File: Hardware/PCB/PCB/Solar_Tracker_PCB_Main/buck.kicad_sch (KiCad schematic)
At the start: 13 parts, among them IC2 TPS54302DDCT

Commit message: Actualizacion PCB Principal
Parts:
- C6: value 75p -> 47p
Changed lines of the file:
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@@
 	(generator_version "9.0")
 	(paper "A4")
+	(text_box "These component values follow the typical application (Figure 8-1, page 14).\nAlternative values are listed in Table 8-2 (page 18) for 3.3 V output.\nThe typical voltage refence (Fb) is 0.596V.\n\nSpecs:\n	Use X7R ceramic capacitors\n	Use resistors with 1% maximum tolerance\n	Use ferrite-core inductors\n\n "
+		(exclude_from_sim no)
+		(at 31.75 139.7 0)
+		(size 85.09 35.56)
+		(margins 0.9525 0.9525 0.9525 0.9525)
+		(stroke
+			(width 0)
+			(type solid)
+		)
+		(fill
+			(type none)
+		)
+		(effects
+			(font
+				(size 1.27 1.27)
+			)
+			(justify left top)
+		)
+	)
 	(junction
 		(at 179.07 80.01)
@@
 		)
 		(instances
-			(project ""
+			(project "Solar_Tracker_PCB_Main"
 				(path "/99b6ddd9-7ffe-4c85-972a-e0f594a166d4/c6e05bfb-9dbb-4b23-9f99-8dd532fd7f1c"
 					(reference "IC2")
@@
 		)
 		(instances
-			(project ""
+			(project "Solar_Tracker_PCB_Main"
 				(path "/99b6ddd9-7ffe-4c85-972a-e0f594a166d4/c6e05bfb-9dbb-4b23-9f99-8dd532fd7f1c"
 					(reference "R6")
@@
 		)
 		(instances
-			(project ""
+			(project "Solar_Tracker_PCB_Main"
 				(path "/99b6ddd9-7ffe-4c85-972a-e0f594a166d4/c6e05bfb-9dbb-4b23-9f99-8dd532fd7f1c"
 					(reference "#PWR013")
@@
 		)
 		(instances
-			(project ""
+			(project "Solar_Tracker_PCB_Main"
 				(path "/99b6ddd9-7ffe-4c85-972a-e0f594a166d4/c6e05bfb-9dbb-4b23-9f99-8dd532fd7f1c"
 					(reference "L1")
@@
 			)
 		)
-		(property "Value" "75p"
+		(property "Value" "47p"
 			(at 173.736 76.962 0)
 			(effects

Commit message: Actualizacion de Footprints Resistencias y Capacitores Main PCB
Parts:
- C10, C11, C6, C7, C8, C9: footprint (none) -> Capacitor_SMD:C_0805_2012Metric_Pad1.18x1.45mm_HandSolder
- L1: footprint (none) -> Inductor_SMD:L_0805_2012Metric_Pad1.05x1.20mm_HandSolder
- R10, R6, R7, R8, R9: footprint (none) -> Resistor_SMD:R_0805_2012Metric_Pad1.20x1.40mm_HandSolder
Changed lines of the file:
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@@
 			)
 		)
-		(property "Footprint" ""
+		(property "Footprint" "Capacitor_SMD:C_0805_2012Metric_Pad1.18x1.45mm_HandSolder"
 			(at 91.1352 87.63 0)
 			(effects
@@
 			)
 		)
-		(property "Footprint" ""
+		(property "Footprint" "Capacitor_SMD:C_0805_2012Metric_Pad1.18x1.45mm_HandSolder"
 			(at 142.24 58.7248 0)
 			(effects
@@
 			)
 		)
-		(property "Footprint" ""
+		(property "Footprint" "Resistor_SMD:R_0805_2012Metric_Pad1.20x1.40mm_HandSolder"
 			(at 184.912 74.93 90)
 			(effects
@@
 			)
 		)
-		(property "Footprint" ""
+		(property "Footprint" "Resistor_SMD:R_0805_2012Metric_Pad1.20x1.40mm_HandSolder"
 			(at 184.912 63.5 90)
 			(effects
@@
 			)
 		)
-		(property "Footprint" ""
+		(property "Footprint" "Resistor_SMD:R_0805_2012Metric_Pad1.20x1.40mm_HandSolder"
 			(at 109.982 92.71 90)
 			(effects
@@
 			)
 		)
-		(property "Footprint" ""
+		(property "Footprint" "Capacitor_SMD:C_0805_2012Metric_Pad1.18x1.45mm_HandSolder"
 			(at 173.6852 67.31 0)
 			(effects
@@
 			)
 		)
-		(property "Footprint" ""
+		(property "Footprint" "Capacitor_SMD:C_0805_2012Metric_Pad1.18x1.45mm_HandSolder"
 			(at 98.7552 87.63 0)
 			(effects
@@
 			)
 		)
-		(property "Footprint" ""
+		(property "Footprint" "Capacitor_SMD:C_0805_2012Metric_Pad1.18x1.45mm_HandSolder"
 			(at 165.4048 59.69 0)
 			(effects
@@
 			)
 		)
-		(property "Footprint" ""
+		(property "Footprint" "Inductor_SMD:L_0805_2012Metric_Pad1.05x1.20mm_HandSolder"
 			(at 158.75 59.69 0)
 			(effects
@@
 			)
 		)
-		(property "Footprint" ""
+		(property "Footprint" "Resistor_SMD:R_0805_2012Metric_Pad1.20x1.40mm_HandSolder"
 			(at 109.982 83.82 90)
 			(effects
@@
 			)
 		)
-		(property "Footprint" ""
+		(property "Footprint" "Resistor_SMD:R_0805_2012Metric_Pad1.20x1.40mm_HandSolder"
 			(at 184.912 85.09 90)
 			(effects
@@
 			)
 		)
-		(property "Footprint" ""
+		(property "Footprint" "Capacitor_SMD:C_0805_2012Metric_Pad1.18x1.45mm_HandSolder"
 			(at 180.0352 77.47 0)
 			(effects

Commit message: Actualizacion Main pcb
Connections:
- net BUCK_VOUT renamed VDD
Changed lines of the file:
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@@
-		)
-	)
-	(global_label "BUCK_VOUT"
-		(shape input)
-		(at 199.39 59.69 0)
-		(fields_autoplaced yes)
-		(effects
-			(font
-				(size 1.27 1.27)
-			)
-			(justify left)
-		)
-		(property "Intersheetrefs" "${INTERSHEET_REFS}"
-			(at 213.2005 59.69 0)
-			(effects
-				(font
-					(size 1.27 1.27)
-				)
-				(justify left)
-				(hide yes)
-			)
 		)
 	)
@@
 					(unit 1)
 				)
+			)
+		)
+	)
+	(symbol
+		(lib_id "power:VDD")
+		(at 199.39 59.69 270)
+		(unit 1)
+		(exclude_from_sim no)
+		(in_bom yes)
+		(on_board yes)
+		(dnp no)
+		(fields_autoplaced yes)
+		(property "Reference" "#PWR060"
+			(at 195.58 59.69 0)
+			(effects
+				(font
+					(size 1.27 1.27)
+				)
+				(hide yes)
+			)
+		)
+		(property "Value" "VDD"
+			(at 203.2 59.6899 90)
+			(effects
+				(font
+					(size 1.27 1.27)
+				)
+				(justify left)
+			)
+		)
+		(property "Footprint" ""
+			(at 199.39 59.69 0)
+			(effects
+				(font
+					(size 1.27 1.27)
+				)
+				(hide yes)
+			)
+		)
+		(property "Datasheet" ""
+			(at 199.39 59.69 0)
+			(effects
+				(font
+					(size 1.27 1.27)
+				)
+				(hide yes)
+			)
+		)
+		(property "Description" "Power symbol creates a global label with name \"VDD\""
+			(at 199.39 59.69 0)
+			(effects
+				(font
+					(size 1.27 1.27)
+				)
+				(hide yes)
+			)
+		)
+		(pin "1"
+		)
+		(instances
+			(project "Solar_Tracker_PCB_Main"
+				(path "/99b6ddd9-7ffe-4c85-972a-e0f594a166d4/c6e05bfb-9dbb-4b23-9f99-8dd532fd7f1c"
+					(reference "#PWR060")
+					(unit 1)
+				)

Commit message: comienzo de distribucion pcb
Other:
- moved on the sheet: C10, C11, C6, C7, C8, C9, IC2, L1, R10, R6, R7, R8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

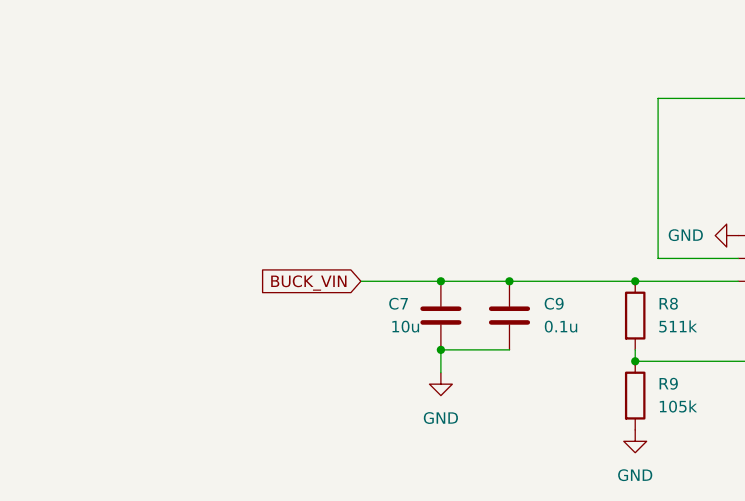
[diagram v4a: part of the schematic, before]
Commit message: Modificaciones PCB MAIN
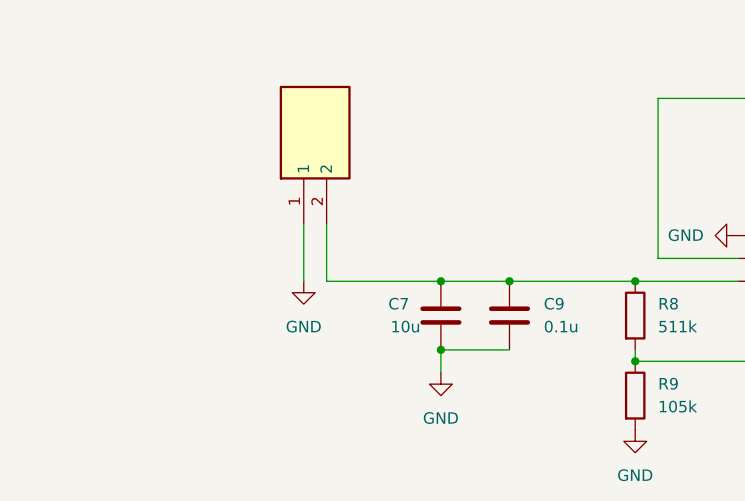
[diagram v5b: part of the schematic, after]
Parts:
- added J7: TB002-500-02BE, TB002:TB00250002BE, symbol TB002-500-02BE:TB002-500-02BE
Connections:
- net GND: now also J7.1
- net BUCK_VIN: no longer names the net of C7.1, C9.1, IC2.3 (VIN), R8.1
- net BUCK_VIN: now also J7.2
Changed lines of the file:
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@@
 	(wire
 		(pts
-			(xy 69.85 88.9) (xy 78.74 88.9)
+			(xy 66.04 88.9) (xy 66.04 82.55)
+		)
+		(stroke
+			(width 0)
+			(type default)
+		)
+	)
+	(wire
+		(pts
+			(xy 66.04 88.9) (xy 78.74 88.9)
 		)
 		(stroke
@@
 	(wire
 		(pts
+			(xy 63.5 82.55) (xy 63.5 88.9)
+		)
+		(stroke
+			(width 0)
+			(type default)
+		)
+	)
+	(wire
+		(pts
 			(xy 175.26 68.58) (xy 187.96 68.58)
 		)
@@
 			(width 0)
 			(type default)
-		)
-	)
-	(global_label "BUCK_VIN"
-		(shape input)
-		(at 69.85 88.9 180)
-		(fields_autoplaced yes)
-		(effects
-			(font
-				(size 1.27 1.27)
-			)
-			(justify right)
-		)
-		(property "Intersheetrefs" "${INTERSHEET_REFS}"
-			(at 57.7328 88.9 0)
-			(effects
-				(font
-					(size 1.27 1.27)
-				)
-				(justify right)
-				(hide yes)
-			)
 		)
 	)
@@
 	)
 	(symbol
+		(lib_id "power:GND")
+		(at 63.5 88.9 0)
+		(unit 1)
+		(exclude_from_sim no)
+		(in_bom yes)
+		(on_board yes)
+		(dnp no)
+		(fields_autoplaced yes)
+		(property "Reference" "#PWR069"
+			(at 63.5 95.25 0)
+			(effects
+				(font
+					(size 1.27 1.27)
+				)
+				(hide yes)
+			)
+		)
+		(property "Value" "GND"
+			(at 63.5 93.98 0)
+			(effects
+				(font
+					(size 1.27 1.27)
+				)
+			)
+		)
+		(property "Footprint" ""
+			(at 63.5 88.9 0)
+			(effects
+				(font
+					(size 1.27 1.27)
+				)
+				(hide yes)
+			)
+		)
+		(property "Datasheet" ""
+			(at 63.5 88.9 0)
+			(effects
+				(font
+					(size 1.27 1.27)
+				)
+				(hide yes)
+			)
+		)
+		(property "Description" "Power symbol creates a global label with name \"GND\" , ground"
+			(at 63.5 88.9 0)
+			(effects
+				(font
+					(size 1.27 1.27)
+				)
+				(hide yes)
+			)
+		)
+		(pin "1"
+		)
+		(instances
+			(project "Solar_Tracker_PCB_Main"
+				(path "/99b6ddd9-7ffe-4c85-972a-e0f594a166d4/c6e05bfb-9dbb-4b23-9f99-8dd532fd7f1c"
+					(reference "#PWR069")
+					(unit 1)
+				)
+			)
+		)
+	)
+	(symbol
 		(lib_id "Device:C")
 		(at 78.74 92.71 0)
@@
 					(unit 1)
 				)
+			)
+		)
+	)
+	(symbol
+		(lib_id "TB002-500-02BE:TB002-500-02BE")
+		(at 63.5 82.55 90)
+		(unit 1)
+		(exclude_from_sim no)
+		(in_bom yes)
+		(on_board yes)
+		(dnp no)
+		(fields_autoplaced yes)
+		(property "Reference" "J7"
+			(at 63.4999 66.04 0)
+			(effects
+				(font
+					(size 1.27 1.27)
+				)
+				(justify left)
+				(hide yes)
+			)
+		)
+		(property "Value" "TB002-500-02BE"
+			(at 66.0399 66.04 0)
+			(effects
+				(font
+					(size 1.27 1.27)
+				)
+				(justify left)
+				(hide yes)
+			)
+		)
+		(property "Footprint" "TB002:TB00250002BE"
+			(at 158.42 66.04 0)
+			(effects
+				(font
+					(size 1.27 1.27)
+				)
+				(justify left top)
+				(hide yes)
+			)
+		)
+		(property "Datasheet" "https://www.sameskydevices.com/product/resource/tb002-500.pdf"
+			(at 258.42 66.04 0)
+			(effects
+				(font
+					(size 1.27 1.27)
+				)
+				(justify left top)
+				(hide yes)
+			)
+		)
+		(property "Description" "TB002-500 Series - 2~24 Poles, Screw Type, Horizontal, 5.0 Pitch, 22~12 (AWG), Terminal Block Connector"
+			(at 63.5 82.55 0)
+			(effects
+				(font
+					(size 1.27 1.27)
+				)
+				(hide yes)
+			)
+		)
+		(property "Height" "10.4"
+			(at 458.42 66.04 0)
+			(effects
+				(font
+					(size 1.27 1.27)
+				)
+				(justify left top)
+				(hide yes)
+			)
+		)
+		(property "Mouser Part Number" "490-TB002-500-02BE"
+			(at 558.42 66.04 0)
+			(effects
+				(font
+					(size 1.27 1.27)
+				)
+				(justify left top)
+				(hide yes)
+			)
+		)
+		(property "Mouser Price/Stock" "https://www.mouser.co.uk/ProductDetail/Same-Sky/TB002-500-02BE?qs=vLWxofP3U2x9716kcgva%2Fw%3D%3D"
+			(at 658.42 66.04 0)
+			(effects
+				(font
+					(size 1.27 1.27)
+				)
+				(justify left top)
+				(hide yes)
+			)
+		)
+		(property "Manufacturer_Name" "Same Sky"
+			(at 758.42 66.04 0)
+			(effects
+				(font
+					(size 1.27 1.27)
+				)
+				(justify left top)
+				(hide yes)
+			)
+		)
+		(property "Manufacturer_Part_Number" "TB002-500-02BE"
+			(at 858.42 66.04 0)
+			(effects
+				(font
+					(size 1.27 1.27)
+				)
+				(justify left top)
+				(hide yes)
+			)
+		)
+		(pin "2"
+		)
+		(pin "1"
+		)
+		(instances
+			(project ""
+				(path "/99b6ddd9-7ffe-4c85-972a-e0f594a166d4/c6e05bfb-9dbb-4b23-9f99-8dd532fd7f1c"
+					(reference "J7")
+					(unit 1)
+				)

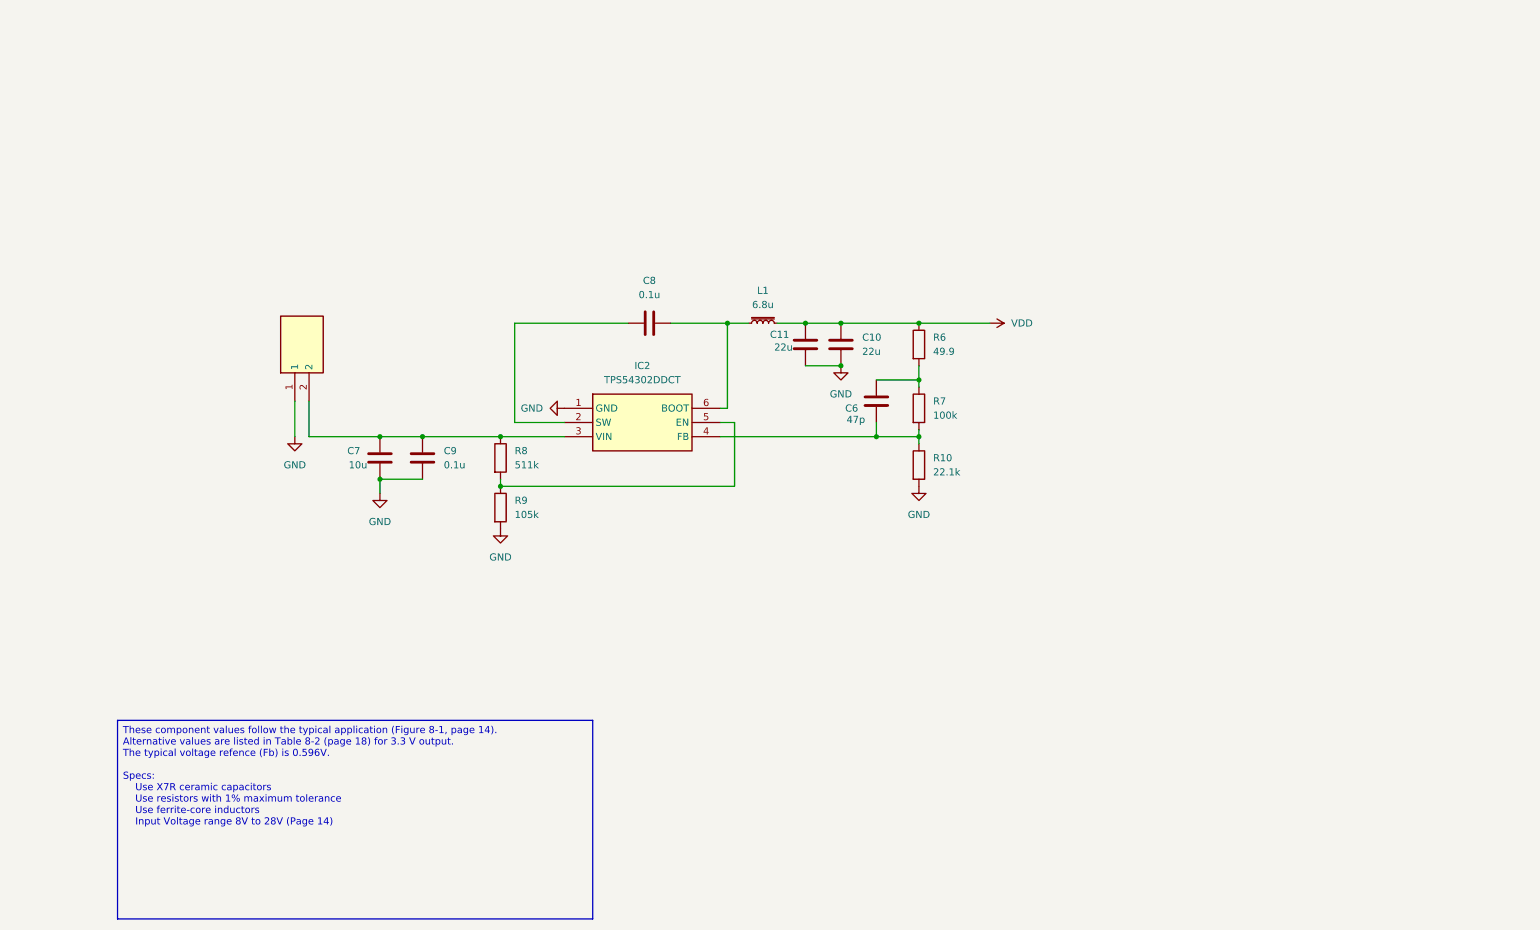
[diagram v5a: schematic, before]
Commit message: Agregue protecciones de polaridad inversa y independencia de fuentes
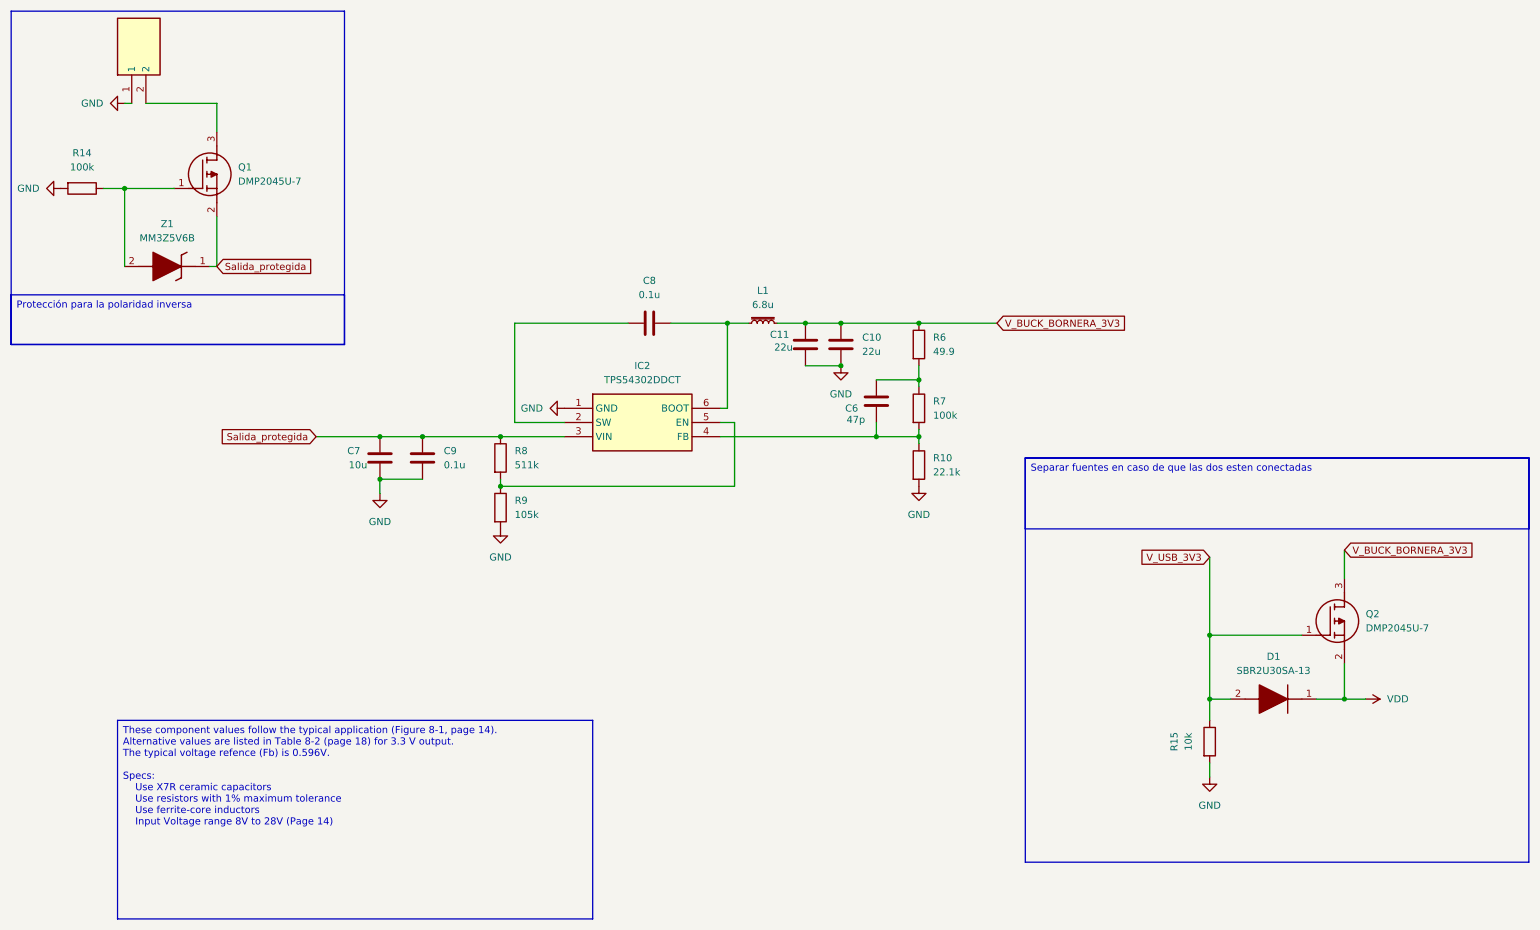
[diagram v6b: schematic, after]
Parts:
- added D1: SBR2U30SA-13, DIOM5226X230N, symbol SBR2U30SA-13:SBR2U30SA-13
- added Q1, Q2: DMP2045U-7, SOT96P240X115-3N, symbol DMP2045U-7:DMP2045U-7
- added R14: 100k, Resistor_SMD:R_0805_2012Metric_Pad1.20x1.40mm_HandSolder, symbol Device:R
- added R15: 10k, Resistor_SMD:R_0805_2012Metric_Pad1.20x1.40mm_HandSolder, symbol Device:R
- added Z1: MM3Z5V6B, SODFL2512X90N, symbol MM3Z5V6B:MM3Z5V6B
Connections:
- net GND: now also R14.2, R15.2
- net VDD: now also D1.1 (K), Q2.2 (S); no longer C10.1, C11.2, L1.2, R6.1
- net Salida_protegida: now reaches C7.1, C9.1, IC2.3 (VIN), R8.1
- net Salida_protegida: now also Q1.2 (S), Z1.1 (K); no longer J7.2
- new net: Q1.1 (G), R14.1, Z1.2 (A)
- new net: J7.2, Q1.3 (D)
- new net V_BUCK_BORNERA_3V3: C10.1, C11.2, L1.2, Q2.3 (D), R6.1
- new net V_USB_3V3: D1.2 (A), Q2.1 (G), R15.1
